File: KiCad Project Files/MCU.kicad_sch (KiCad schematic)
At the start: 24 parts, among them SW1 Reset, Y1 12MHz

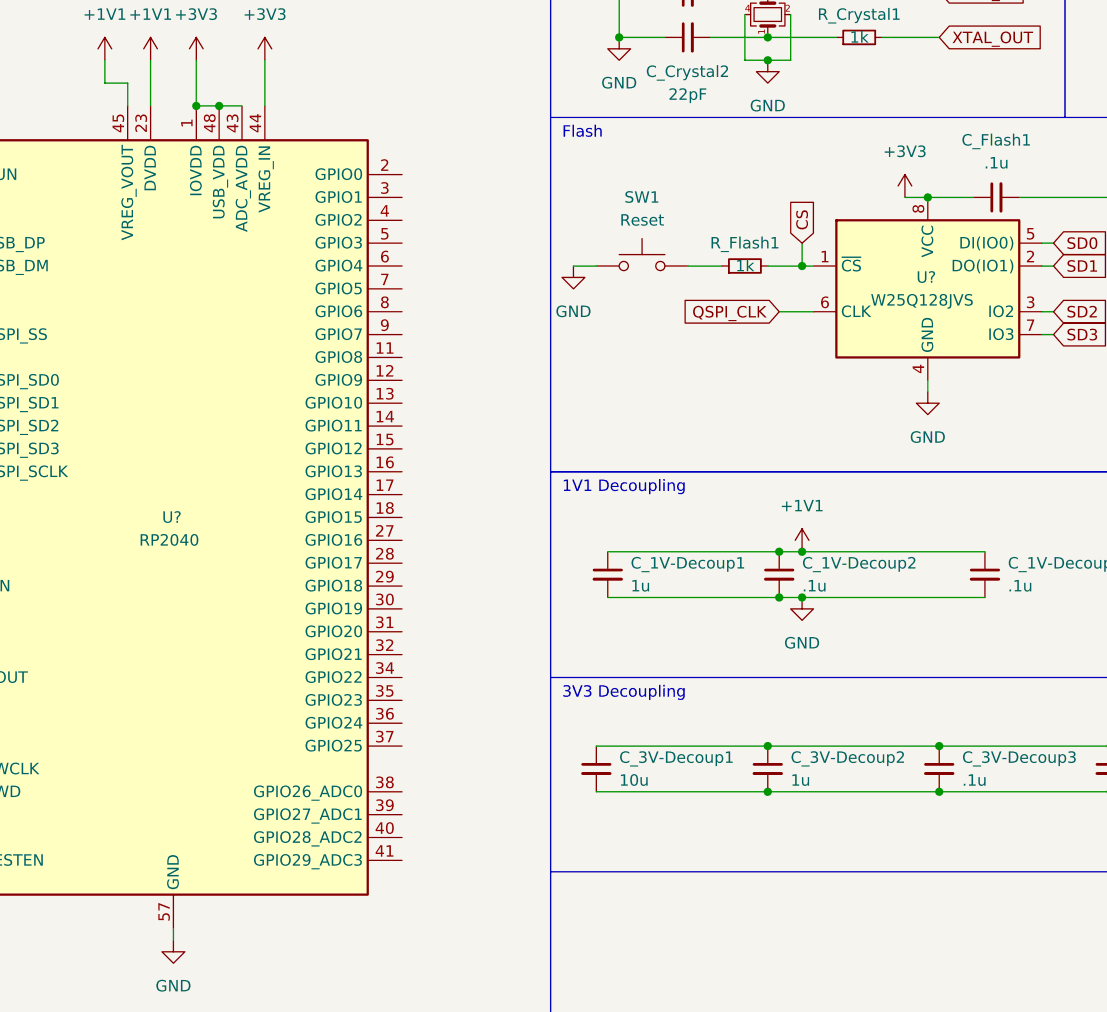
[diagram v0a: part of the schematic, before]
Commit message: Finish schematic, annotate footprints, start pcb creation
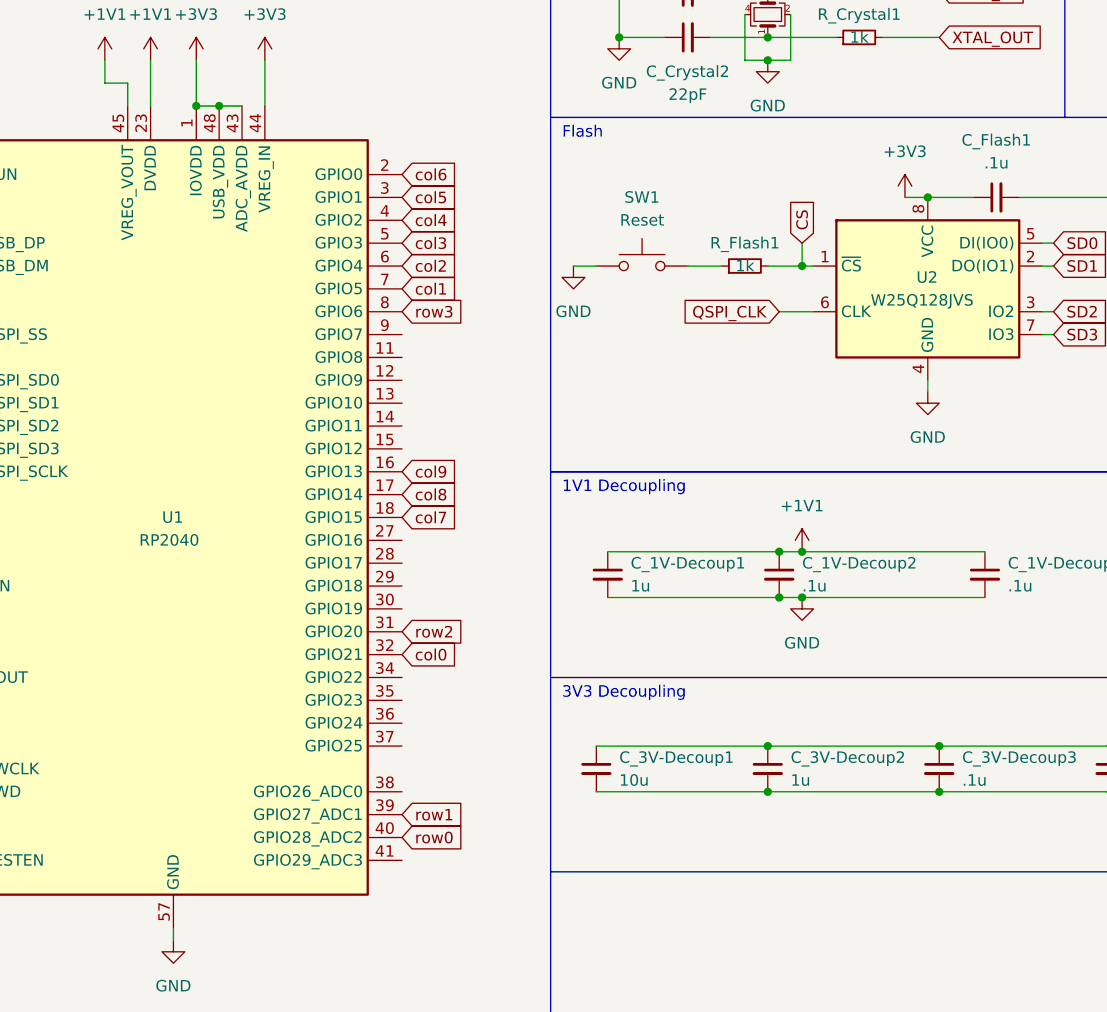
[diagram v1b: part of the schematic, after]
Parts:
- C_1V-Decoup1, C_1V-Decoup2, C_1V-Decoup3, C_3V-Decoup1, C_3V-Decoup2, C_3V-Decoup3, C_3V-Decoup4, C_3V-Decoup5, C_3V-Decoup6, C_3V-Decoup7, C_3V-Decoup8, C_3V-Decoup9, C_Crystal1, C_Crystal2, C_Flash1: footprint (none) -> Capacitor_SMD:C_0402_1005Metric
- R_Crystal1, R_DATA1, R_DATA2, R_Flash1, R_RST1: footprint (none) -> Resistor_SMD:R_0402_1005Metric
- SW1: footprint (none) -> Connector_PinHeader_1.27mm:PinHeader_1x02_P1.27mm_Vertical
- Y1: footprint (none) -> Crystal:Crystal_SMD_3225-4Pin_3.2x2.5mm
- gave numbers to parts that had none: 2
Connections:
- net col9: now reaches U1.16 (GPIO13)
- net col8: now reaches U1.17 (GPIO14)
- net col7: now reaches U1.18 (GPIO15)
- net col6: now reaches U1.2 (GPIO0)
- net col5: now reaches U1.3 (GPIO1)
- net row2: now reaches U1.31 (GPIO20)
- net col0: now reaches U1.32 (GPIO21)
- net row1: now reaches U1.39 (GPIO27_ADC1)
- net col4: now reaches U1.4 (GPIO2)
- net row0: now reaches U1.40 (GPIO28_ADC2)
- net col3: now reaches U1.5 (GPIO3)
- net col2: now reaches U1.6 (GPIO4)
- net col1: now reaches U1.7 (GPIO5)
- net row3: now reaches U1.8 (GPIO6)

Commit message: Finish PCB and create production files
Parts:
- U1: footprint Package_DFN_QFN:QFN-56-1EP_7x7mm_P0.4mm_EP3.2x3.2mm -> cipulot_parts:RP2040-QFN-56
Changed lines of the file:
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@@
       (effects (font (size 1.27 1.27)) (justify left))
     )
-    (property "Footprint" "Package_DFN_QFN:QFN-56-1EP_7x7mm_P0.4mm_EP3.2x3.2mm" (id 2) (at 63.5 81.28 0)
+    (property "Footprint" "cipulot_parts:RP2040-QFN-56" (id 2) (at 63.5 81.28 0)
       (effects (font (size 1.27 1.27)) hide)
     )
